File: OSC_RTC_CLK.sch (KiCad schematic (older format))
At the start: 8 parts

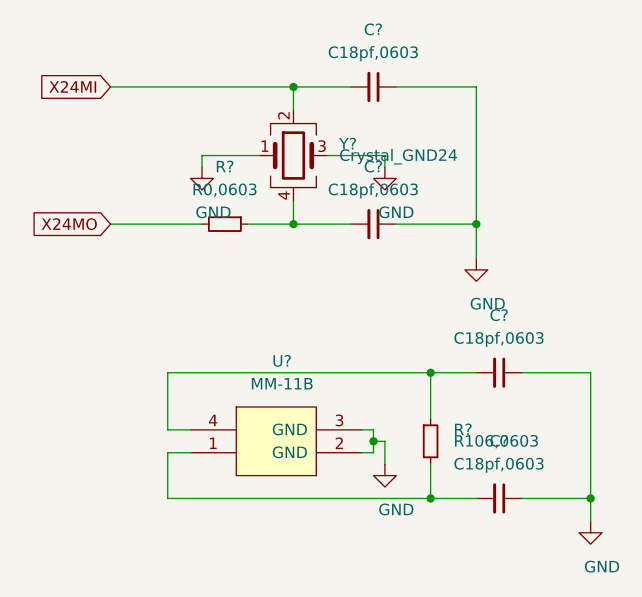
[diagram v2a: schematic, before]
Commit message: update X32k global label,
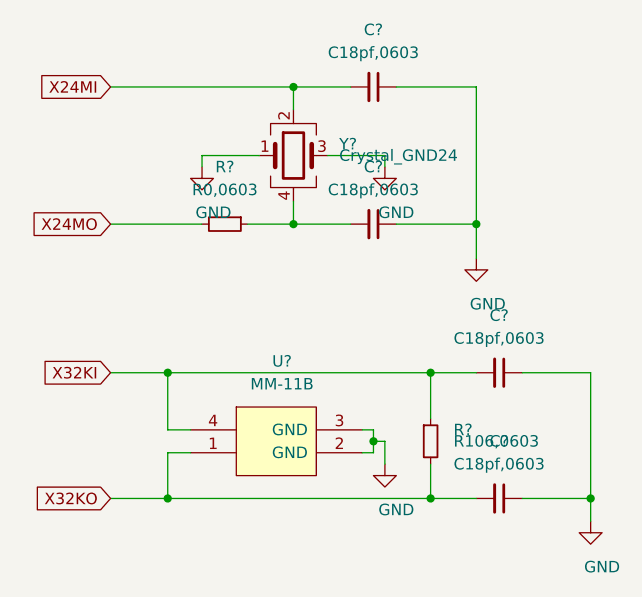
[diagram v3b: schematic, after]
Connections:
- net X32KO: now reaches C?.2, R?.2, U?.1
- net X32KI: now reaches C?.2, R?.1, U?.4
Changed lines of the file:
@@
 $Descr A3 16535 11693
 encoding utf-8
-Sheet 20 34
+Sheet 21 34
 Title ""
 Date ""
@@
 Wire Wire Line
 	9600 5350 9600 4800
+Text GLabel 7500 4800 0    50   Input ~ 0
+X32KI
+Text GLabel 7500 5350 0    50   Input ~ 0
+X32KO
+Wire Wire Line
+	7500 4800 7750 4800
+Connection ~ 7750 4800
+Wire Wire Line
+	7500 5350 7750 5350
+Connection ~ 7750 5350
 $EndSCHEMATC
